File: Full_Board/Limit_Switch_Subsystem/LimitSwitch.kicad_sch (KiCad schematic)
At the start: 7 parts, among them J9 OQ0212500000G

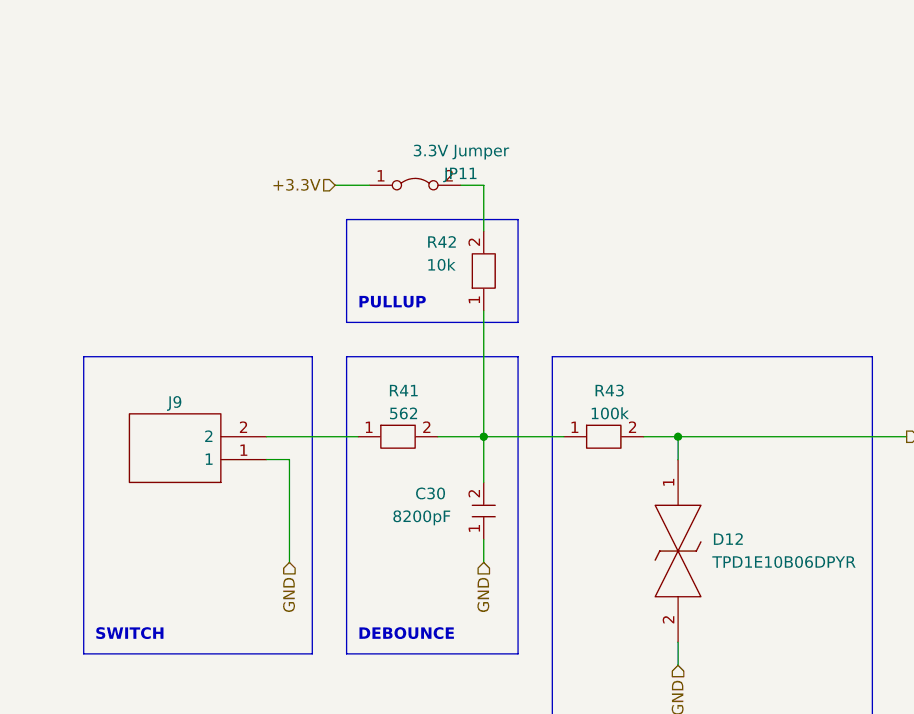
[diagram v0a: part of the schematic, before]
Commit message: Added USB connector for the pi
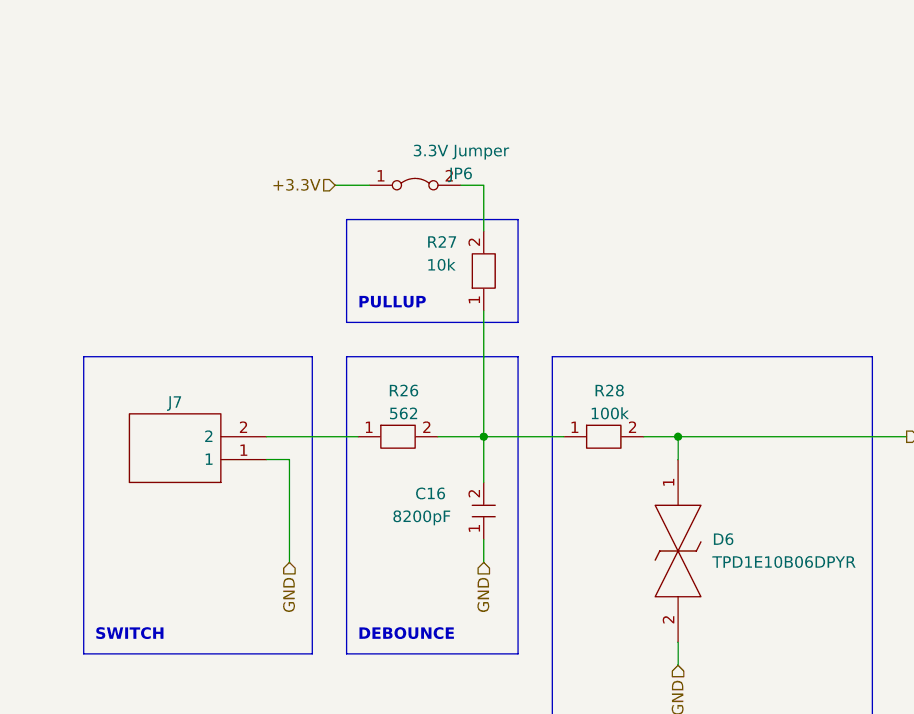
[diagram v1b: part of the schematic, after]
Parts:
- renumbered C30 to C16, D12 to D6, J9 to J7, JP11 to JP6, R41 to R26, R42 to R27, R43 to R28
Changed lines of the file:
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@@
     (effects (font (size 1.27 1.27)) (justify right))
   )
-  (symbol (lib_id "OQ0212500000G:OQ0212500000G") (at 119.38 92.71 180) (unit 1)
-    (in_bom yes) (on_board yes)
-    (property "Reference" "J9" (id 0) (at 109.22 86.36 0))
+  (symbol (lib_id "OQ0212500000G:OQ0212500000G") (at 119.38 92.71 180)
+    (in_bom yes) (on_board yes)
+    (property "Reference" "J7" (id 0) (at 109.22 86.36 0))
     (property "Value" "OQ0212500000G" (id 1) (at 109.22 85.09 0)
       (effects (font (size 1.27 1.27)) hide)
@@
     (pin "2")
   )
-  (symbol (lib_id "CR0402-FX-5620GLF:CR0402-FX-5620GLF") (at 129.54 90.17 0) (unit 1)
-    (in_bom yes) (on_board yes)
-    (property "Reference" "R41" (id 0) (at 134.62 85.09 0))
+  (symbol (lib_id "CR0402-FX-5620GLF:CR0402-FX-5620GLF") (at 129.54 90.17 0)
+    (in_bom yes) (on_board yes)
+    (property "Reference" "R26" (id 0) (at 134.62 85.09 0))
     (property "Value" "562" (id 1) (at 134.62 87.63 0))
     (property "Footprint" "CR0402-FX-5620GLF:RESC1005X40N" (id 2) (at 143.51 88.9 0)
@@
     (pin "2")
   )
-  (symbol (lib_id "RMCF1206FT10K0:10k") (at 143.51 76.2 90) (unit 1)
-    (in_bom yes) (on_board yes)
-    (property "Reference" "R42" (id 0) (at 137.16 68.58 90)
+  (symbol (lib_id "RMCF1206FT10K0:10k") (at 143.51 76.2 90)
+    (in_bom yes) (on_board yes)
+    (property "Reference" "R27" (id 0) (at 137.16 68.58 90)
       (effects (font (size 1.27 1.27)) (justify right))
     )
@@
     (pin "2")
   )
-  (symbol (lib_id "RCV2512100KFKEGAT:RCV2512100KFKEGAT") (at 152.4 90.17 0) (unit 1)
-    (in_bom yes) (on_board yes)
-    (property "Reference" "R43" (id 0) (at 157.48 85.09 0))
+  (symbol (lib_id "RCV2512100KFKEGAT:RCV2512100KFKEGAT") (at 152.4 90.17 0)
+    (in_bom yes) (on_board yes)
+    (property "Reference" "R28" (id 0) (at 157.48 85.09 0))
     (property "Value" "100k" (id 1) (at 157.48 87.63 0))
     (property "Footprint" "RCV2512100KFKEGAT:RESC6332X70N" (id 2) (at 166.37 88.9 0)
@@
     (pin "2")
   )
-  (symbol (lib_id "C1210C822K2RACAUTO:C1210C822K2RACAUTO") (at 143.51 101.6 90) (unit 1)
-    (in_bom yes) (on_board yes)
-    (property "Reference" "C30" (id 0) (at 135.89 96.52 90)
+  (symbol (lib_id "C1210C822K2RACAUTO:C1210C822K2RACAUTO") (at 143.51 101.6 90)
+    (in_bom yes) (on_board yes)
+    (property "Reference" "C16" (id 0) (at 135.89 96.52 90)
       (effects (font (size 1.27 1.27)) (justify right))
     )
@@
     (pin "2")
   )
-  (symbol (lib_id "Jumper:Jumper_2_Bridged") (at 135.89 62.23 0) (unit 1)
-    (in_bom yes) (on_board yes)
-    (property "Reference" "JP11" (id 0) (at 140.97 60.96 0))
+  (symbol (lib_id "Jumper:Jumper_2_Bridged") (at 135.89 62.23 0)
+    (in_bom yes) (on_board yes)
+    (property "Reference" "JP6" (id 0) (at 140.97 60.96 0))
     (property "Value" "3.3V Jumper" (id 1) (at 140.97 58.42 0))
     (property "Footprint" "TestPoint:TestPoint_2Pads_Pitch2.54mm_Drill0.8mm" (id 2) (at 135.89 62.23 0)
@@
     (pin "2")
   )
-  (symbol (lib_id "TPD1E10B06DPYR:TPD1E10B06DPYR") (at 165.1 92.71 270) (unit 1)
-    (in_bom yes) (on_board yes)
-    (property "Reference" "D12" (id 0) (at 168.91 101.6 90)
+  (symbol (lib_id "TPD1E10B06DPYR:TPD1E10B06DPYR") (at 165.1 92.71 270)
+    (in_bom yes) (on_board yes)
+    (property "Reference" "D6" (id 0) (at 168.91 101.6 90)
       (effects (font (size 1.27 1.27)) (justify left))
     )

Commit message: pcb_layout_v2
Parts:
- renumbered C16 to C30, D6 to D12, J7 to J9, JP6 to JP11, R26 to R41, R27 to R42, R28 to R43
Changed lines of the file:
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@@
     (effects (font (size 1.27 1.27)) (justify right))
   )
-  (symbol (lib_id "OQ0212500000G:OQ0212500000G") (at 119.38 92.71 180)
-    (in_bom yes) (on_board yes)
-    (property "Reference" "J7" (id 0) (at 109.22 86.36 0))
+  (symbol (lib_id "OQ0212500000G:OQ0212500000G") (at 119.38 92.71 180) (unit 1)
+    (in_bom yes) (on_board yes)
+    (property "Reference" "J9" (id 0) (at 109.22 86.36 0))
     (property "Value" "OQ0212500000G" (id 1) (at 109.22 85.09 0)
       (effects (font (size 1.27 1.27)) hide)
@@
     (pin "2")
   )
-  (symbol (lib_id "CR0402-FX-5620GLF:CR0402-FX-5620GLF") (at 129.54 90.17 0)
-    (in_bom yes) (on_board yes)
-    (property "Reference" "R26" (id 0) (at 134.62 85.09 0))
+  (symbol (lib_id "CR0402-FX-5620GLF:CR0402-FX-5620GLF") (at 129.54 90.17 0) (unit 1)
+    (in_bom yes) (on_board yes)
+    (property "Reference" "R41" (id 0) (at 134.62 85.09 0))
     (property "Value" "562" (id 1) (at 134.62 87.63 0))
     (property "Footprint" "CR0402-FX-5620GLF:RESC1005X40N" (id 2) (at 143.51 88.9 0)
@@
     (pin "2")
   )
-  (symbol (lib_id "RMCF1206FT10K0:10k") (at 143.51 76.2 90)
-    (in_bom yes) (on_board yes)
-    (property "Reference" "R27" (id 0) (at 137.16 68.58 90)
+  (symbol (lib_id "RMCF1206FT10K0:10k") (at 143.51 76.2 90) (unit 1)
+    (in_bom yes) (on_board yes)
+    (property "Reference" "R42" (id 0) (at 137.16 68.58 90)
       (effects (font (size 1.27 1.27)) (justify right))
     )
@@
     (pin "2")
   )
-  (symbol (lib_id "RCV2512100KFKEGAT:RCV2512100KFKEGAT") (at 152.4 90.17 0)
-    (in_bom yes) (on_board yes)
-    (property "Reference" "R28" (id 0) (at 157.48 85.09 0))
+  (symbol (lib_id "RCV2512100KFKEGAT:RCV2512100KFKEGAT") (at 152.4 90.17 0) (unit 1)
+    (in_bom yes) (on_board yes)
+    (property "Reference" "R43" (id 0) (at 157.48 85.09 0))
     (property "Value" "100k" (id 1) (at 157.48 87.63 0))
     (property "Footprint" "RCV2512100KFKEGAT:RESC6332X70N" (id 2) (at 166.37 88.9 0)
@@
     (pin "2")
   )
-  (symbol (lib_id "C1210C822K2RACAUTO:C1210C822K2RACAUTO") (at 143.51 101.6 90)
-    (in_bom yes) (on_board yes)
-    (property "Reference" "C16" (id 0) (at 135.89 96.52 90)
+  (symbol (lib_id "C1210C822K2RACAUTO:C1210C822K2RACAUTO") (at 143.51 101.6 90) (unit 1)
+    (in_bom yes) (on_board yes)
+    (property "Reference" "C30" (id 0) (at 135.89 96.52 90)
       (effects (font (size 1.27 1.27)) (justify right))
     )
@@
     (pin "2")
   )
-  (symbol (lib_id "Jumper:Jumper_2_Bridged") (at 135.89 62.23 0)
-    (in_bom yes) (on_board yes)
-    (property "Reference" "JP6" (id 0) (at 140.97 60.96 0))
+  (symbol (lib_id "Jumper:Jumper_2_Bridged") (at 135.89 62.23 0) (unit 1)
+    (in_bom yes) (on_board yes)
+    (property "Reference" "JP11" (id 0) (at 140.97 60.96 0))
     (property "Value" "3.3V Jumper" (id 1) (at 140.97 58.42 0))
     (property "Footprint" "TestPoint:TestPoint_2Pads_Pitch2.54mm_Drill0.8mm" (id 2) (at 135.89 62.23 0)
@@
     (pin "2")
   )
-  (symbol (lib_id "TPD1E10B06DPYR:TPD1E10B06DPYR") (at 165.1 92.71 270)
-    (in_bom yes) (on_board yes)
-    (property "Reference" "D6" (id 0) (at 168.91 101.6 90)
+  (symbol (lib_id "TPD1E10B06DPYR:TPD1E10B06DPYR") (at 165.1 92.71 270) (unit 1)
+    (in_bom yes) (on_board yes)
+    (property "Reference" "D12" (id 0) (at 168.91 101.6 90)
       (effects (font (size 1.27 1.27)) (justify left))
     )

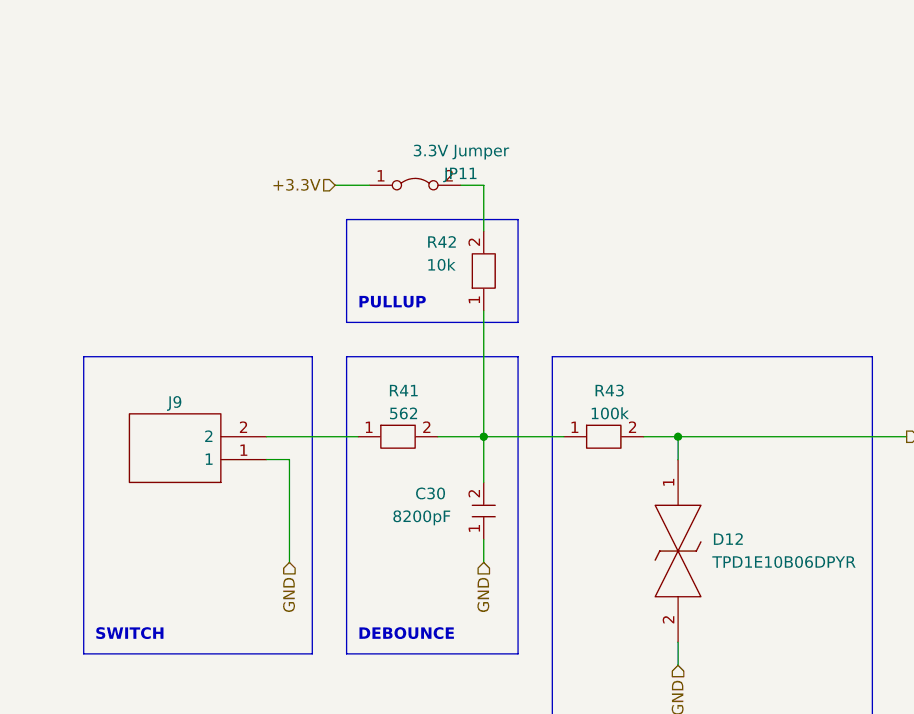
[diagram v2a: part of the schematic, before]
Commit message: Swapped pins on the barrel jack
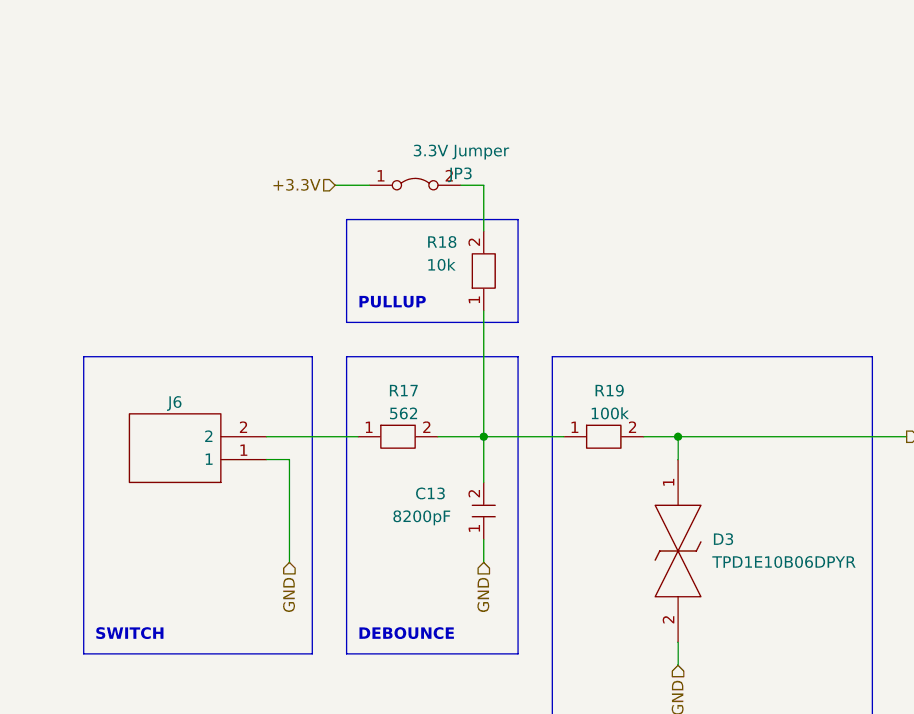
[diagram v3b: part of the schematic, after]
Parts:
- renumbered C30 to C13, D12 to D3, J9 to J6, JP11 to JP3, R41 to R17, R42 to R18, R43 to R19
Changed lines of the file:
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@@
     (effects (font (size 1.27 1.27)) (justify right))
   )
-  (symbol (lib_id "OQ0212500000G:OQ0212500000G") (at 119.38 92.71 180) (unit 1)
-    (in_bom yes) (on_board yes)
-    (property "Reference" "J9" (id 0) (at 109.22 86.36 0))
+  (symbol (lib_id "OQ0212500000G:OQ0212500000G") (at 119.38 92.71 180)
+    (in_bom yes) (on_board yes)
+    (property "Reference" "J6" (id 0) (at 109.22 86.36 0))
     (property "Value" "OQ0212500000G" (id 1) (at 109.22 85.09 0)
       (effects (font (size 1.27 1.27)) hide)
@@
     (pin "2")
   )
-  (symbol (lib_id "CR0402-FX-5620GLF:CR0402-FX-5620GLF") (at 129.54 90.17 0) (unit 1)
-    (in_bom yes) (on_board yes)
-    (property "Reference" "R41" (id 0) (at 134.62 85.09 0))
+  (symbol (lib_id "CR0402-FX-5620GLF:CR0402-FX-5620GLF") (at 129.54 90.17 0)
+    (in_bom yes) (on_board yes)
+    (property "Reference" "R17" (id 0) (at 134.62 85.09 0))
     (property "Value" "562" (id 1) (at 134.62 87.63 0))
     (property "Footprint" "CR0402-FX-5620GLF:RESC1005X40N" (id 2) (at 143.51 88.9 0)
@@
     (pin "2")
   )
-  (symbol (lib_id "RMCF1206FT10K0:10k") (at 143.51 76.2 90) (unit 1)
-    (in_bom yes) (on_board yes)
-    (property "Reference" "R42" (id 0) (at 137.16 68.58 90)
+  (symbol (lib_id "RMCF1206FT10K0:10k") (at 143.51 76.2 90)
+    (in_bom yes) (on_board yes)
+    (property "Reference" "R18" (id 0) (at 137.16 68.58 90)
       (effects (font (size 1.27 1.27)) (justify right))
     )
@@
     (pin "2")
   )
-  (symbol (lib_id "RCV2512100KFKEGAT:RCV2512100KFKEGAT") (at 152.4 90.17 0) (unit 1)
-    (in_bom yes) (on_board yes)
-    (property "Reference" "R43" (id 0) (at 157.48 85.09 0))
+  (symbol (lib_id "RCV2512100KFKEGAT:RCV2512100KFKEGAT") (at 152.4 90.17 0)
+    (in_bom yes) (on_board yes)
+    (property "Reference" "R19" (id 0) (at 157.48 85.09 0))
     (property "Value" "100k" (id 1) (at 157.48 87.63 0))
     (property "Footprint" "RCV2512100KFKEGAT:RESC6332X70N" (id 2) (at 166.37 88.9 0)
@@
     (pin "2")
   )
-  (symbol (lib_id "C1210C822K2RACAUTO:C1210C822K2RACAUTO") (at 143.51 101.6 90) (unit 1)
-    (in_bom yes) (on_board yes)
-    (property "Reference" "C30" (id 0) (at 135.89 96.52 90)
+  (symbol (lib_id "C1210C822K2RACAUTO:C1210C822K2RACAUTO") (at 143.51 101.6 90)
+    (in_bom yes) (on_board yes)
+    (property "Reference" "C13" (id 0) (at 135.89 96.52 90)
       (effects (font (size 1.27 1.27)) (justify right))
     )
@@
     (pin "2")
   )
-  (symbol (lib_id "Jumper:Jumper_2_Bridged") (at 135.89 62.23 0) (unit 1)
-    (in_bom yes) (on_board yes)
-    (property "Reference" "JP11" (id 0) (at 140.97 60.96 0))
+  (symbol (lib_id "Jumper:Jumper_2_Bridged") (at 135.89 62.23 0)
+    (in_bom yes) (on_board yes)
+    (property "Reference" "JP3" (id 0) (at 140.97 60.96 0))
     (property "Value" "3.3V Jumper" (id 1) (at 140.97 58.42 0))
     (property "Footprint" "TestPoint:TestPoint_2Pads_Pitch2.54mm_Drill0.8mm" (id 2) (at 135.89 62.23 0)
@@
     (pin "2")
   )
-  (symbol (lib_id "TPD1E10B06DPYR:TPD1E10B06DPYR") (at 165.1 92.71 270) (unit 1)
-    (in_bom yes) (on_board yes)
-    (property "Reference" "D12" (id 0) (at 168.91 101.6 90)
+  (symbol (lib_id "TPD1E10B06DPYR:TPD1E10B06DPYR") (at 165.1 92.71 270)
+    (in_bom yes) (on_board yes)
+    (property "Reference" "D3" (id 0) (at 168.91 101.6 90)
       (effects (font (size 1.27 1.27)) (justify left))
     )

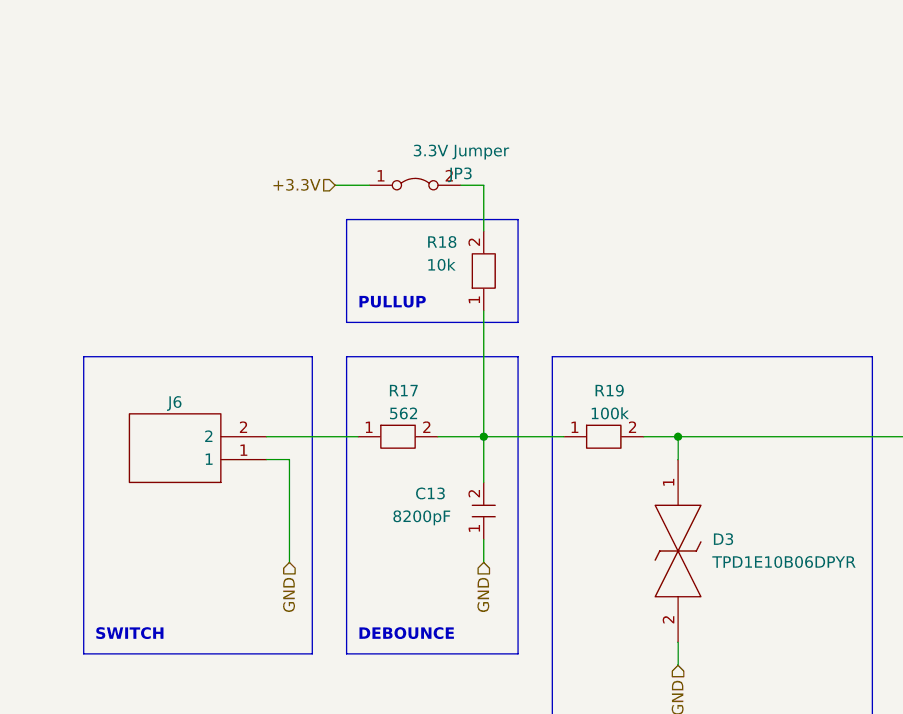
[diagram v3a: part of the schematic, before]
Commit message: Layed out power supply
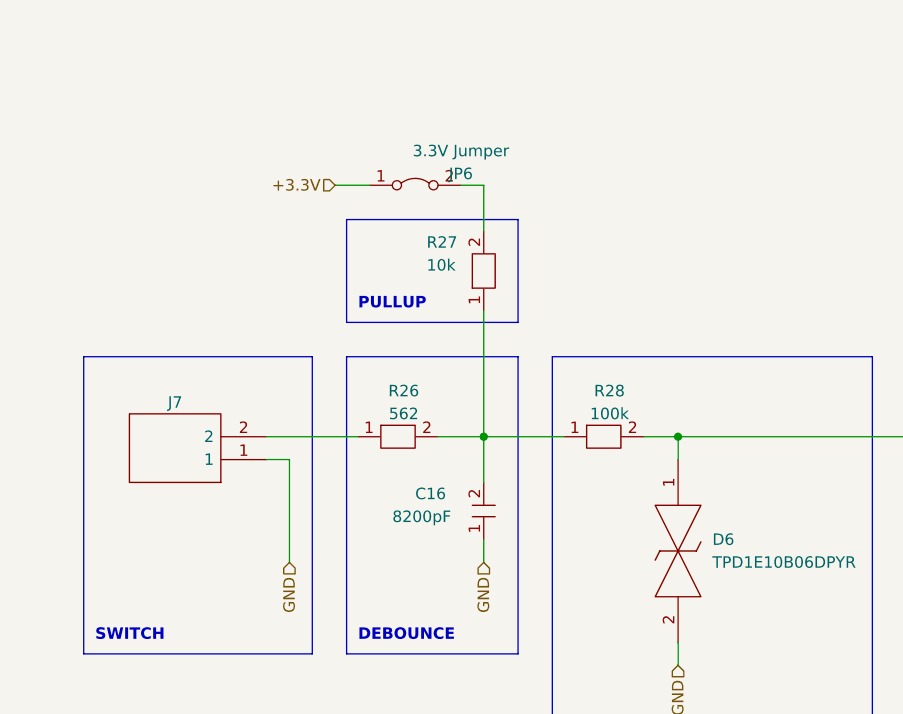
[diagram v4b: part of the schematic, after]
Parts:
- renumbered C13 to C16, D3 to D6, J6 to J7, JP3 to JP6, R17 to R26, R18 to R27, R19 to R28
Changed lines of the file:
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@@
   (symbol (lib_id "OQ0212500000G:OQ0212500000G") (at 119.38 92.71 180)
     (in_bom yes) (on_board yes)
-    (property "Reference" "J6" (id 0) (at 109.22 86.36 0))
+    (property "Reference" "J7" (id 0) (at 109.22 86.36 0))
     (property "Value" "OQ0212500000G" (id 1) (at 109.22 85.09 0)
       (effects (font (size 1.27 1.27)) hide)
@@
   (symbol (lib_id "CR0402-FX-5620GLF:CR0402-FX-5620GLF") (at 129.54 90.17 0)
     (in_bom yes) (on_board yes)
-    (property "Reference" "R17" (id 0) (at 134.62 85.09 0))
+    (property "Reference" "R26" (id 0) (at 134.62 85.09 0))
     (property "Value" "562" (id 1) (at 134.62 87.63 0))
     (property "Footprint" "CR0402-FX-5620GLF:RESC1005X40N" (id 2) (at 143.51 88.9 0)
@@
   (symbol (lib_id "RMCF1206FT10K0:10k") (at 143.51 76.2 90)
     (in_bom yes) (on_board yes)
-    (property "Reference" "R18" (id 0) (at 137.16 68.58 90)
+    (property "Reference" "R27" (id 0) (at 137.16 68.58 90)
       (effects (font (size 1.27 1.27)) (justify right))
     )
@@
   (symbol (lib_id "RCV2512100KFKEGAT:RCV2512100KFKEGAT") (at 152.4 90.17 0)
     (in_bom yes) (on_board yes)
-    (property "Reference" "R19" (id 0) (at 157.48 85.09 0))
+    (property "Reference" "R28" (id 0) (at 157.48 85.09 0))
     (property "Value" "100k" (id 1) (at 157.48 87.63 0))
     (property "Footprint" "RCV2512100KFKEGAT:RESC6332X70N" (id 2) (at 166.37 88.9 0)
@@
   (symbol (lib_id "C1210C822K2RACAUTO:C1210C822K2RACAUTO") (at 143.51 101.6 90)
     (in_bom yes) (on_board yes)
-    (property "Reference" "C13" (id 0) (at 135.89 96.52 90)
+    (property "Reference" "C16" (id 0) (at 135.89 96.52 90)
       (effects (font (size 1.27 1.27)) (justify right))
     )
@@
   (symbol (lib_id "Jumper:Jumper_2_Bridged") (at 135.89 62.23 0)
     (in_bom yes) (on_board yes)
-    (property "Reference" "JP3" (id 0) (at 140.97 60.96 0))
+    (property "Reference" "JP6" (id 0) (at 140.97 60.96 0))
     (property "Value" "3.3V Jumper" (id 1) (at 140.97 58.42 0))
     (property "Footprint" "TestPoint:TestPoint_2Pads_Pitch2.54mm_Drill0.8mm" (id 2) (at 135.89 62.23 0)
@@
   (symbol (lib_id "TPD1E10B06DPYR:TPD1E10B06DPYR") (at 165.1 92.71 270)
     (in_bom yes) (on_board yes)
-    (property "Reference" "D3" (id 0) (at 168.91 101.6 90)
+    (property "Reference" "D6" (id 0) (at 168.91 101.6 90)
       (effects (font (size 1.27 1.27)) (justify left))
     )
